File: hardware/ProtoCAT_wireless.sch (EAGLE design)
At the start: 67 parts, among them Q1 MOSFET-NCHANNELSMD, Q2 MOSFET-NCHANNELSMD, U1 ARDUINO, U3 TB6612FNG

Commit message: Updated XBee footprint and added RESET control
Added RESET for XBee and fixed PWR lines to the XBee
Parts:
- added JP20: M02PTH, SparkFun-Connectors:M02PTH
- added R11: 1k, SparkFun-Resistors:1KOHM1/10W1%(0603)
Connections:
- removed net 5V: R10.2, R13.2
- net 3.3V: now also R11.2
- net GND: now also JP20.1
- net VCC: now also R10.2, R13.2
- net XBEE_RESET: now also JP20.2, R11.1
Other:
- note added: "Power Solder Jumpers"
- note added: "XBee Breakout"
- moved on the sheet: JP23, MOD1, Q1, Q2, R10, R12, R13, R9, SJ3, SJ4

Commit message: Numerous minor edits
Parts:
- added F3: PTCSMD, SparkFun-PowerIC:PTCSMD
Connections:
- removed net FUSED_VCC: C2.1, F2.2, SJ1.3, SJ2.3, U3.STBY, U3.VCC
- removed net VCC: F2.1, R10.2, R13.2, U1.5V
- new net 5V: F2.1, U1.5V
- new net FUSED_3.3V: F3.2, JP23.2, MOD1.VDD, Q1.G, Q2.G, R11.2, R12.2, R6.1, R7.1, R9.2
- new net FUSED_5V: C2.1, F2.2, R10.2, R13.2, SJ1.3, SJ2.3, U3.STBY, U3.VCC
- net 3.3V: now also F3.1; no longer JP23.2, MOD1.VDD, Q1.G, Q2.G, R11.2, R12.2, R6.1, R7.1, R9.2
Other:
- moved on the sheet: C1, C2, C4, F1, F2, JP0, JP1, JP10, JP11, JP12, JP13, JP14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

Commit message: Switched TX / RX lines on XBee
Fixed the Switched TX / RX lines from XBee to Arduino on the HW Serial
lines.

Moved the thru-hole mounts for the Motors to below the SMD mount.

Fixed LEDs for RSSI, DIN / DOUT
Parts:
- removed JP20: M02PTH, SparkFun-Connectors:M02PTH
- added SJ5: SOLDERJUMPERNO, SparkFun-Retired:SOLDERJUMPERNO
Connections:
- removed net D0_RXI: JP0.3, S3.4, U1.RX
- removed net D1_TXO: JP1.3, S3.1, U1.TX
- new net D0/RXI: JP0.3, S3.1, U1.RX
- new net D1/TXO: JP1.3, S3.4, U1.TX
- net A0/SW_RXI: now also S3.3; no longer S3.6
- net A1/SW_TXO: now also S3.6; no longer S3.3
- net GND: now also SJ5.2; no longer JP20.1
- net XBEE_RESET: now also SJ5.1; no longer JP20.2
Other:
- note added: "v12"
- note removed: "v11"
- moved on the sheet: R11
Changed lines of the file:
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@@
 <?xml version="1.0" encoding="utf-8"?>
 <!DOCTYPE eagle SYSTEM "eagle.dtd">
-<eagle version="6.4">
+<eagle version="6.5.0">
 <drawing>
 <settings>
@@
 <part name="SJ4" library="SparkFun-Passives" deviceset="JUMPER-PAD-3-NC_BY_TRACE" device=""/>
 <part name="FRAME1" library="SparkFun-Aesthetics" deviceset="FRAME-LEDGER" device=""/>
-<part name="JP20" library="SparkFun-Connectors" deviceset="M02" device="PTH"/>
 <part name="GND4" library="SparkFun-Aesthetics" deviceset="GND" device=""/>
 <part name="R11" library="SparkFun-Resistors" deviceset="1KOHM1/10W1%(0603)" device="" value="1k"/>
 <part name="F3" library="SparkFun-PowerIC" deviceset="PTC" device="SMD" value="PTCSMD"/>
+<part name="SJ5" library="SparkFun-Retired" deviceset="SOLDERJUMPER" device="NO"/>
 </parts>
 <sheets>
@@
 <wire x1="259.08" y1="205.74" x2="259.08" y2="158.75" width="0.2032" layer="94" style="longdash"/>
 <text x="337.82" y="7.62" size="2.54" layer="94">B. Huang</text>
-<text x="419.1" y="12.7" size="2.54" layer="94">v11</text>
+<text x="419.1" y="7.62" size="2.54" layer="94">v12</text>
 <wire x1="259.08" y1="158.75" x2="259.08" y2="121.92" width="0.2032" layer="94" style="longdash"/>
 <wire x1="259.08" y1="121.92" x2="259.08" y2="0" width="0.2032" layer="94" style="longdash"/>
@@
 <instance part="FRAME1" gate="G$1" x="0" y="0"/>
 <instance part="FRAME1" gate="G$2" x="330.2" y="0"/>
-<instance part="JP20" gate="G$1" x="17.78" y="139.7"/>
 <instance part="GND4" gate="1" x="33.02" y="129.54"/>
-<instance part="R11" gate="G$1" x="27.94" y="149.86" rot="R90"/>
+<instance part="R11" gate="G$1" x="12.7" y="152.4" rot="R90"/>
 <instance part="F3" gate="G$1" x="294.64" y="231.14"/>
+<instance part="SJ5" gate="1" x="17.78" y="139.7"/>
 </instances>
 <busses>
@@
 </segment>
 <segment>
-<pinref part="JP20" gate="G$1" pin="1"/>
-<wire x1="25.4" y1="139.7" x2="33.02" y2="139.7" width="0.1524" layer="91"/>
+<wire x1="22.86" y1="139.7" x2="33.02" y2="139.7" width="0.1524" layer="91"/>
 <wire x1="33.02" y1="139.7" x2="33.02" y2="132.08" width="0.1524" layer="91"/>
 <pinref part="GND4" gate="1" pin="GND"/>
+<pinref part="SJ5" gate="1" pin="2"/>
 </segment>
 </net>
@@
 <net name="RSSI" class="0">
 <segment>
-<wire x1="35.56" y1="55.88" x2="35.56" y2="63.5" width="0.1524" layer="91"/>
-<label x="35.56" y="58.42" size="1.778" layer="95" rot="R90"/>
+<wire x1="35.56" y1="55.88" x2="35.56" y2="60.96" width="0.1524" layer="91"/>
+<label x="35.56" y="60.96" size="1.27" layer="95" rot="R90" xref="yes"/>
 <pinref part="R8" gate="G$1" pin="2"/>
 </segment>
@@
 <net name="A1/SW_TXO" class="0">
 <segment>
+<pinref part="U1" gate="G$1" pin="A1"/>
+<wire x1="327.66" y1="208.28" x2="322.58" y2="208.28" width="0.1524" layer="91"/>
+<label x="322.58" y="208.28" size="1.27" layer="95" rot="R180" xref="yes"/>
+</segment>
+<segment>
+<pinref part="JP15" gate="G$1" pin="3"/>
+<wire x1="218.44" y1="165.1" x2="231.14" y2="165.1" width="0.1524" layer="91"/>
+<label x="231.14" y="165.1" size="1.778" layer="95" xref="yes"/>
+</segment>
+<segment>
+<pinref part="S3" gate="G$1" pin="6"/>
+<wire x1="86.36" y1="38.1" x2="88.9" y2="38.1" width="0.1524" layer="91"/>
+<label x="88.9" y="38.1" size="1.27" layer="95" xref="yes"/>
+</segment>
+</net>
+<net name="A0/SW_RXI" class="0">
+<segment>
+<pinref part="U1" gate="G$1" pin="A0"/>
+<wire x1="327.66" y1="210.82" x2="322.58" y2="210.82" width="0.1524" layer="91"/>
+<label x="322.58" y="210.82" size="1.27" layer="95" rot="R180" xref="yes"/>
+</segment>
+<segment>
+<wire x1="218.44" y1="180.34" x2="231.14" y2="180.34" width="0.1524" layer="91"/>
+<pinref part="JP14" gate="G$1" pin="3"/>
+<label x="231.14" y="180.34" size="1.778" layer="95" xref="yes"/>
+</segment>
+<segment>
 <pinref part="S3" gate="G$1" pin="3"/>
 <wire x1="86.36" y1="45.72" x2="88.9" y2="45.72" width="0.1524" layer="91"/>
 <label x="88.9" y="45.72" size="1.27" layer="95" xref="yes"/>
-</segment>
-<segment>
-<pinref part="U1" gate="G$1" pin="A1"/>
-<wire x1="327.66" y1="208.28" x2="322.58" y2="208.28" width="0.1524" layer="91"/>
-<label x="322.58" y="208.28" size="1.27" layer="95" rot="R180" xref="yes"/>
-</segment>
-<segment>
-<pinref part="JP15" gate="G$1" pin="3"/>
-<wire x1="218.44" y1="165.1" x2="231.14" y2="165.1" width="0.1524" layer="91"/>
-<label x="231.14" y="165.1" size="1.778" layer="95" xref="yes"/>
-</segment>
-</net>
-<net name="A0/SW_RXI" class="0">
-<segment>
-<pinref part="S3" gate="G$1" pin="6"/>
-<wire x1="86.36" y1="38.1" x2="88.9" y2="38.1" width="0.1524" layer="91"/>
-<label x="88.9" y="38.1" size="1.27" layer="95" xref="yes"/>
-</segment>
-<segment>
-<pinref part="U1" gate="G$1" pin="A0"/>
-<wire x1="327.66" y1="210.82" x2="322.58" y2="210.82" width="0.1524" layer="91"/>
-<label x="322.58" y="210.82" size="1.27" layer="95" rot="R180" xref="yes"/>
-</segment>
-<segment>
-<wire x1="218.44" y1="180.34" x2="231.14" y2="180.34" width="0.1524" layer="91"/>
-<pinref part="JP14" gate="G$1" pin="3"/>
-<label x="231.14" y="180.34" size="1.778" layer="95" xref="yes"/>
-</segment>
-</net>
-<net name="D0_RXI" class="0">
-<segment>
-<pinref part="S3" gate="G$1" pin="4"/>
-<wire x1="86.36" y1="43.18" x2="88.9" y2="43.18" width="0.1524" layer="91"/>
-<label x="88.9" y="43.18" size="1.27" layer="95" xref="yes"/>
-</segment>
-<segment>
-<pinref part="U1" gate="G$1" pin="RX"/>
-<wire x1="353.06" y1="210.82" x2="360.68" y2="210.82" width="0.1524" layer="91"/>
-<label x="360.68" y="210.82" size="1.27" layer="95" xref="yes"/>
-</segment>
-<segment>
-<pinref part="JP0" gate="G$1" pin="3"/>
-<wire x1="142.24" y1="177.8" x2="154.94" y2="177.8" width="0.1524" layer="91"/>
-<label x="154.94" y="177.8" size="1.778" layer="95" xref="yes"/>
-</segment>
-</net>
-<net name="D1_TXO" class="0">
-<segment>
-<pinref part="S3" gate="G$1" pin="1"/>
-<wire x1="86.36" y1="50.8" x2="88.9" y2="50.8" width="0.1524" layer="91"/>
-<label x="88.9" y="50.8" size="1.27" layer="95" xref="yes"/>
-</segment>
-<segment>
-<pinref part="U1" gate="G$1" pin="TX"/>
-<wire x1="353.06" y1="208.28" x2="360.68" y2="208.28" width="0.1524" layer="91"/>
-<label x="360.68" y="208.28" size="1.27" layer="95" xref="yes"/>
-</segment>
-<segment>
-<wire x1="142.24" y1="162.56" x2="154.94" y2="162.56" width="0.1524" layer="91"/>
-<pinref part="JP1" gate="G$1" pin="3"/>
-<label x="154.94" y="162.56" size="1.778" layer="95" xref="yes"/>
 </segment>
 </net>
@@
 </segment>
 <segment>
-<pinref part="JP20" gate="G$1" pin="2"/>
-<wire x1="25.4" y1="142.24" x2="27.94" y2="142.24" width="0.1524" layer="91"/>
-<label x="33.02" y="142.24" size="1.27" layer="95" xref="yes"/>
+<label x="10.16" y="144.78" size="1.27" layer="95" rot="R180" xref="yes"/>
 <pinref part="R11" gate="G$1" pin="1"/>
-<wire x1="27.94" y1="142.24" x2="33.02" y2="142.24" width="0.1524" layer="91"/>
-<wire x1="27.94" y1="144.78" x2="27.94" y2="142.24" width="0.1524" layer="91"/>
-<junction x="27.94" y="142.24"/>
+<wire x1="12.7" y1="144.78" x2="10.16" y2="144.78" width="0.1524" layer="91"/>
+<wire x1="12.7" y1="147.32" x2="12.7" y2="144.78" width="0.1524" layer="91"/>
+<pinref part="SJ5" gate="1" pin="1"/>
+<wire x1="12.7" y1="139.7" x2="12.7" y2="144.78" width="0.1524" layer="91"/>
+<junction x="12.7" y="144.78"/>
 </segment>
 </net>
@@
 <segment>
 <wire x1="12.7" y1="38.1" x2="12.7" y2="30.48" width="0.1524" layer="91"/>
-<label x="12.7" y="30.48" size="1.778" layer="95" rot="R90"/>
+<label x="12.7" y="30.48" size="1.27" layer="95" rot="R270" xref="yes"/>
 <pinref part="LED7" gate="G$1" pin="C"/>
 </segment>
@@
 <segment>
 <wire x1="22.86" y1="38.1" x2="22.86" y2="30.48" width="0.1524" layer="91"/>
-<label x="22.86" y="30.48" size="1.778" layer="95" rot="R90"/>
+<label x="22.86" y="30.48" size="1.27" layer="95" rot="R270" xref="yes"/>
 <pinref part="LED8" gate="G$1" pin="C"/>
 </segment>
@@
 <segment>
 <pinref part="R11" gate="G$1" pin="2"/>
-<wire x1="27.94" y1="157.48" x2="27.94" y2="154.94" width="0.1524" layer="91"/>
-<label x="30.48" y="157.48" size="1.27" layer="95" xref="yes"/>
-<wire x1="27.94" y1="157.48" x2="30.48" y2="157.48" width="0.1524" layer="91"/>
+<wire x1="12.7" y1="160.02" x2="12.7" y2="157.48" width="0.1524" layer="91"/>
+<label x="10.16" y="160.02" size="1.27" layer="95" rot="R180" xref="yes"/>
+<wire x1="12.7" y1="160.02" x2="10.16" y2="160.02" width="0.1524" layer="91"/>
 </segment>
 <segment>
@@
 </segment>
 </net>
+<net name="D0/RXI" class="0">
+<segment>
+<pinref part="JP0" gate="G$1" pin="3"/>
+<wire x1="142.24" y1="177.8" x2="154.94" y2="177.8" width="0.1524" layer="91"/>
+<label x="154.94" y="177.8" size="1.778" layer="95" xref="yes"/>
+</segment>
+<segment>
+<pinref part="S3" gate="G$1" pin="1"/>
+<wire x1="86.36" y1="50.8" x2="88.9" y2="50.8" width="0.1524" layer="91"/>
+<label x="88.9" y="50.8" size="1.27" layer="95" xref="yes"/>
+</segment>
+<segment>
+<pinref part="U1" gate="G$1" pin="RX"/>
+<wire x1="353.06" y1="210.82" x2="360.68" y2="210.82" width="0.1524" layer="91"/>
+<label x="360.68" y="210.82" size="1.27" layer="95" xref="yes"/>
+</segment>
+</net>
+<net name="D1/TXO" class="0">
+<segment>
+<wire x1="142.24" y1="162.56" x2="154.94" y2="162.56" width="0.1524" layer="91"/>
+<pinref part="JP1" gate="G$1" pin="3"/>
+<label x="154.94" y="162.56" size="1.778" layer="95" xref="yes"/>
+</segment>
+<segment>
+<pinref part="S3" gate="G$1" pin="4"/>
+<wire x1="86.36" y1="43.18" x2="88.9" y2="43.18" width="0.1524" layer="91"/>
+<label x="88.9" y="43.18" size="1.27" layer="95" xref="yes"/>
+</segment>
+<segment>
+<pinref part="U1" gate="G$1" pin="TX"/>
+<wire x1="353.06" y1="208.28" x2="360.68" y2="208.28" width="0.1524" layer="91"/>
+<label x="360.68" y="208.28" size="1.27" layer="95" xref="yes"/>
+</segment>
+</net>

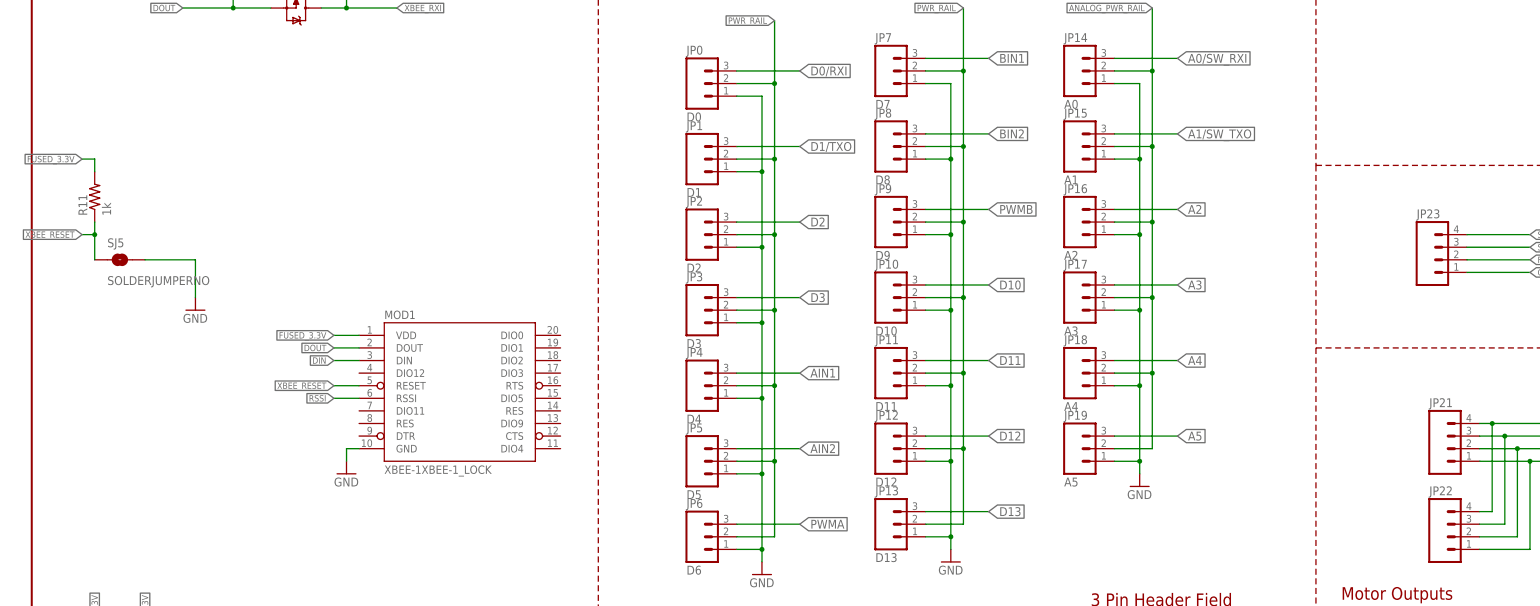
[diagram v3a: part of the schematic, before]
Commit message: Added break-out for 4 I/O pins on XBee
Added breakout pins for DIO0, DIO1, P0, P1 and GND to the board.
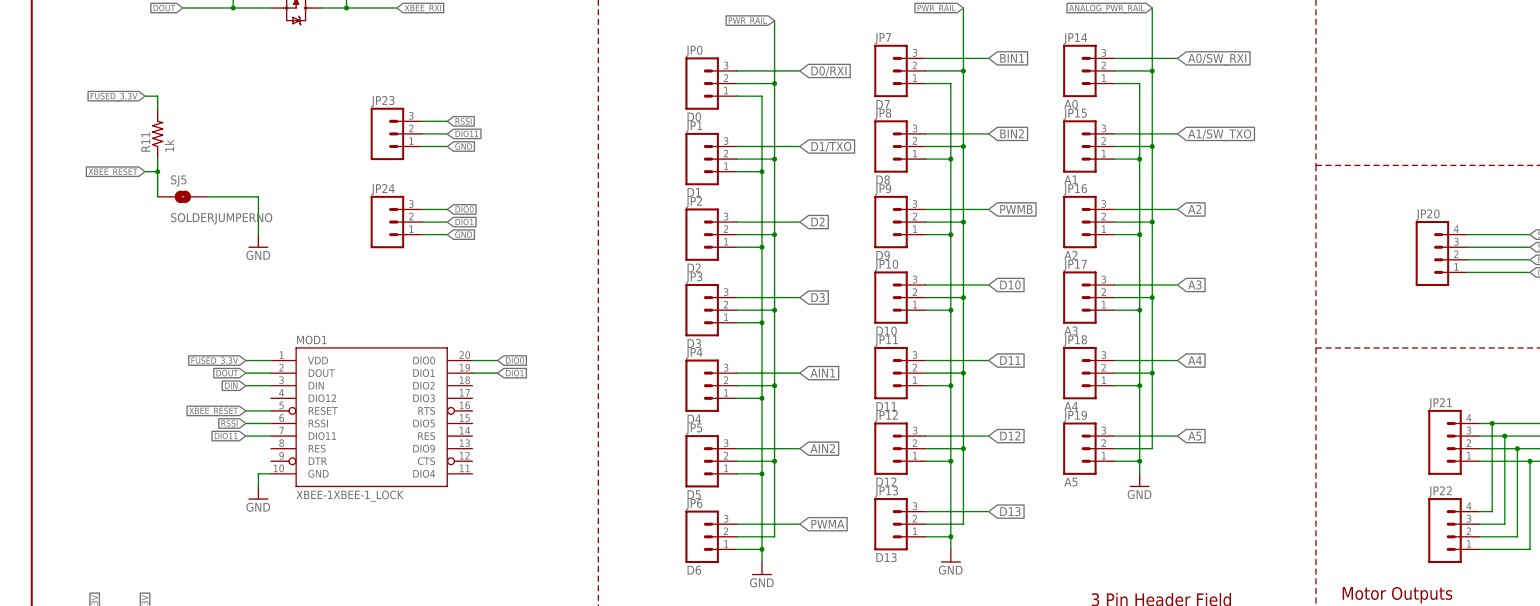
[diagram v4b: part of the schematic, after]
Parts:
- added JP20: (no value), SparkFun-Connectors:M04PTH
- added JP24: (no value), SparkFun-Connectors:M031X03_NO_SILK
- JP23: device SparkFun-Connectors:M04PTH -> SparkFun-Connectors:M031X03_NO_SILK
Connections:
- new net DIO0: JP24.3, MOD1.DIO0
- new net DIO1: JP24.2, MOD1.DIO1
- new net DIO11: JP23.2, MOD1.DIO11
- net FUSED_3.3V: now also JP20.2; no longer JP23.2
- net GND: now also JP20.1, JP24.1
- net RSSI: now also JP23.3
- net SCL_I2C_PORT: now also JP20.4; no longer JP23.4
- net SDA_I2C_PORT: now also JP20.3; no longer JP23.3
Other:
- moved on the sheet: MOD1, R11, SJ5
